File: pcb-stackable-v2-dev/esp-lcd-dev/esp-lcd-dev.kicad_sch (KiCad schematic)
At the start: 27 parts, among them J1 JST XH/PH, J2 Qwiic, J3 Qwiic, J4 STEMMA-Signal, J5 JST SH, J6 Pin headers, Q1 2N7002DW, U1 VEML7700

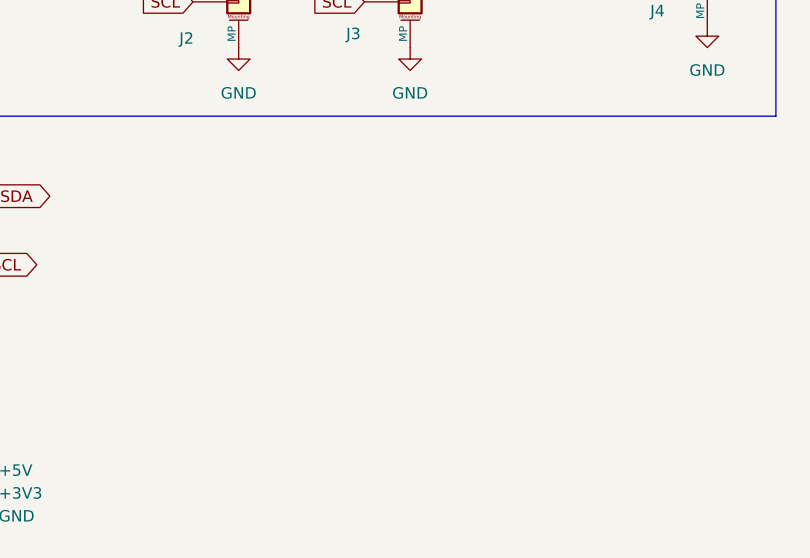
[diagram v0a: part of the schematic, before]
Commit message: Add SMD pin sockets for LCD module on esp-lcd-dev
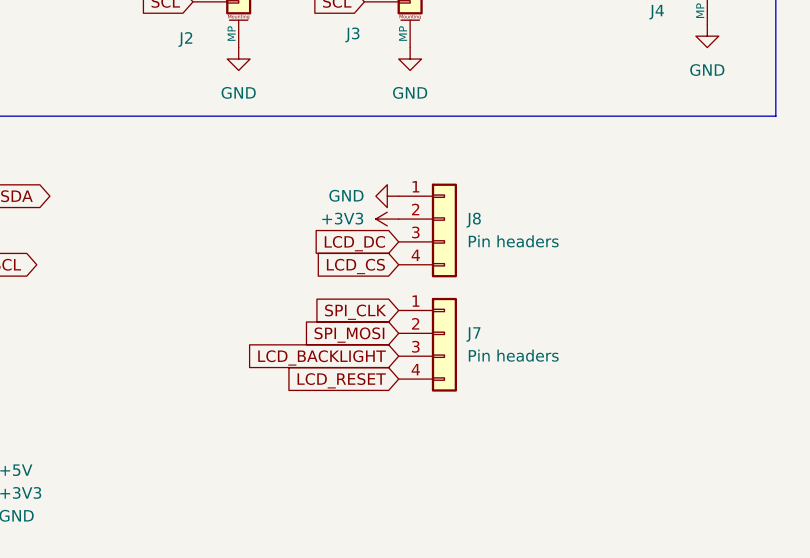
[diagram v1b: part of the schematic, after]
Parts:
- added J7: Pin headers, Connector_PinSocket_2.54mm:PinSocket_1x04_P2.54mm_Vertical_SMD_Pin1Right, symbol Connector_Generic:Conn_01x04
- added J8: Pin headers, Connector_PinSocket_2.54mm:PinSocket_1x04_P2.54mm_Vertical_SMD_Pin1Left, symbol Connector_Generic:Conn_01x04
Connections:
- net +3V3: now also J8.2 (Pin_2)
- net GND: now also J8.1 (Pin_1)
- net LCD_BACKLIGHT: now also J7.3 (Pin_3)
- net LCD_CS: now also J8.4 (Pin_4)
- net LCD_DC: now also J8.3 (Pin_3)
- net LCD_RESET: now also J7.4 (Pin_4)
- net SPI_CLK: now also J7.1 (Pin_1)
- net SPI_MOSI: now also J7.2 (Pin_2)
